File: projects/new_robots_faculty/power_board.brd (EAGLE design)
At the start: 117 x 120.6 mm, 46 parts

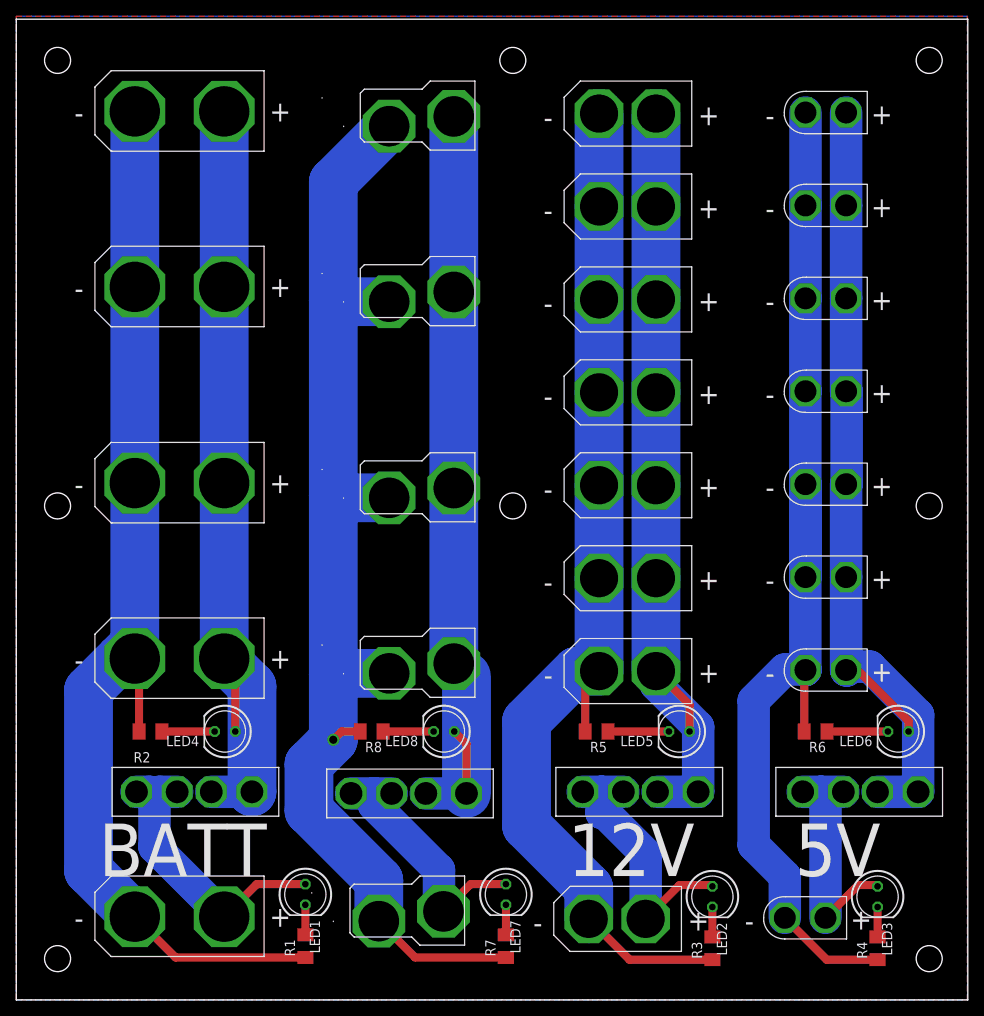
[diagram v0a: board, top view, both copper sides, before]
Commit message: updated power_board
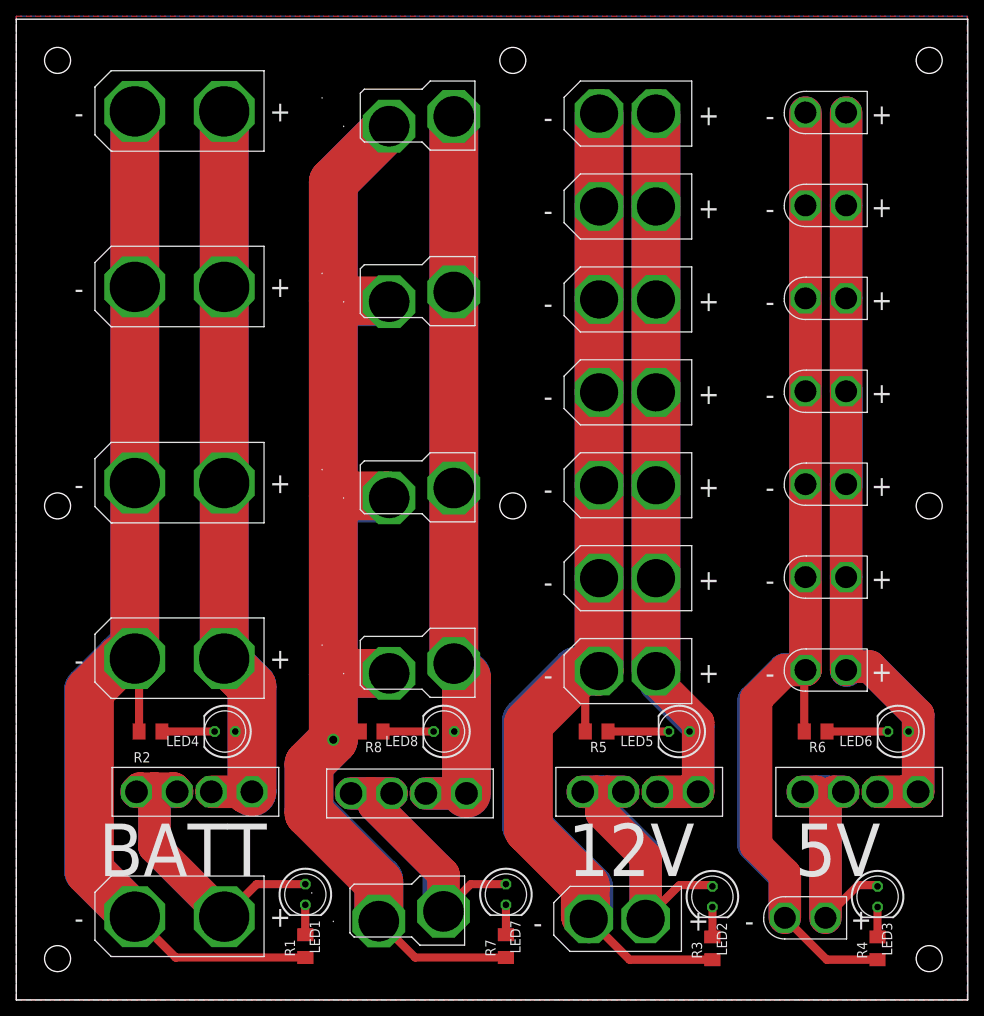
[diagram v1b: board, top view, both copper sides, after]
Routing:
- net N$11: track 147.5 -> 273.8 mm
- net 12V_MINUS: track 133.0 -> 240.0 mm
- net BATT_MINUS: track 137.8 -> 242.4 mm
- net 5V_MINUS: track 137.5 -> 242.0 mm
- net 5V_PLUS: track 106.2 -> 196.0 mm
- net N$12: track 97.2 -> 186.9 mm
- net BATT_PLUS: track 99.7 -> 185.3 mm
- net 12V_PLUS: track 99.7 -> 185.1 mm
- net BATT_RAW: track 35.4 -> 60.1 mm
- net N$9: track 32.4 -> 55.7 mm
- net 12V_RAW: track 33.1 -> 55.9 mm
- net 5V_RAW: track 28.9 -> 48.5 mm
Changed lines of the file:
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@@
 <?xml version="1.0" encoding="utf-8"?>
 <!DOCTYPE eagle SYSTEM "eagle.dtd">
-<eagle version="9.3.2">
+<eagle version="9.6.2">
 <drawing>
 <settings>
@@
 <wire x1="15.11" y1="33.02" x2="15.11" y2="41.46" width="1" layer="1"/>
 <wire x1="15.11" y1="41.46" x2="14.58" y2="41.99" width="1" layer="1"/>
+<wire x1="14.58" y1="10.24" x2="9" y2="15.82" width="6" layer="1"/>
+<wire x1="9" y1="38" x2="13" y2="42" width="6" layer="1"/>
+<wire x1="13" y1="42" x2="14.57" y2="42" width="6" layer="1"/>
+<wire x1="14.57" y1="42" x2="14.58" y2="41.99" width="6" layer="1"/>
+<wire x1="9" y1="15.82" x2="9" y2="38" width="6" layer="1"/>
+<wire x1="14.58" y1="63.58" x2="14.58" y2="41.99" width="6" layer="1"/>
+<wire x1="14.58" y1="63.58" x2="14.58" y2="109.3" width="6" layer="1"/>
 </signal>
 <signal name="BATT_RAW">
@@
 <wire x1="19.79" y1="25.6" x2="17.6" y2="25.6" width="4" layer="16"/>
 <wire x1="17.6" y1="25.6" x2="17" y2="25" width="4" layer="16"/>
+<wire x1="25.58" y1="10.24" x2="17" y2="18.82" width="4" layer="1"/>
+<wire x1="17" y1="18.82" x2="17" y2="26" width="4" layer="1"/>
+<wire x1="17" y1="26" x2="15.19" y2="26" width="4" layer="1"/>
+<wire x1="15.19" y1="26" x2="14.79" y2="25.6" width="4" layer="1"/>
+<wire x1="19.79" y1="25.6" x2="19.39" y2="26" width="4" layer="1"/>
+<wire x1="19.39" y1="26" x2="17" y2="26" width="4" layer="1"/>
 </signal>
 <signal name="BATT_PLUS">
@@
 <contactref element="U$21" pad="C"/>
 <wire x1="25.58" y1="41.99" x2="25.58" y2="63.58" width="6" layer="16"/>
-<wire x1="25.552" y1="41.962" x2="25.58" y2="41.99" width="1" layer="1"/>
 <contactref element="LED4" pad="A"/>
 <wire x1="26.94" y1="33.02" x2="26.94" y2="40.574" width="1" layer="1"/>
 <wire x1="26.94" y1="40.574" x2="25.552" y2="41.962" width="1" layer="1"/>
-<wire x1="23.99" y1="25.6" x2="28.99" y2="25.6" width="4" layer="16"/>
 <wire x1="28.99" y1="25.6" x2="29" y2="25.61" width="6" layer="16"/>
 <wire x1="29" y1="38.57" x2="25.58" y2="41.99" width="6" layer="16"/>
@@
 <wire x1="25.58" y1="109.3" x2="25.58" y2="87.71" width="6" layer="16"/>
 <wire x1="25.58" y1="87.71" x2="25.58" y2="63.58" width="6" layer="16"/>
+<wire x1="25.58" y1="109.3" x2="25.58" y2="41.99" width="6" layer="1"/>
+<wire x1="25.58" y1="41.99" x2="25.552" y2="41.962" width="6" layer="1"/>
+<wire x1="28.99" y1="25.6" x2="28.99" y2="38.524" width="6" layer="1"/>
+<wire x1="28.99" y1="38.524" x2="25.552" y2="41.962" width="6" layer="1"/>
+<wire x1="23.99" y1="25.6" x2="27.4" y2="25.6" width="4" layer="1"/>
+<wire x1="27.4" y1="25.6" x2="28" y2="25" width="4" layer="1"/>
+<wire x1="28" y1="25" x2="28.39" y2="25" width="4" layer="1"/>
+<wire x1="28.39" y1="25" x2="28.99" y2="25.6" width="4" layer="1"/>
 </signal>
 <signal name="N$5">
@@
 <wire x1="72.39" y1="23" x2="72" y2="23" width="4" layer="16"/>
 <wire x1="72" y1="23" x2="72" y2="25.6" width="4" layer="16"/>
+<wire x1="77.42" y1="9.97" x2="77.42" y2="17.58" width="4" layer="1"/>
+<wire x1="77.42" y1="17.58" x2="72" y2="23" width="4" layer="1"/>
+<wire x1="72" y1="23" x2="72" y2="25" width="4" layer="1"/>
+<wire x1="72" y1="25" x2="71.4" y2="25.6" width="4" layer="1"/>
+<wire x1="71.4" y1="25.6" x2="69.68" y2="25.6" width="4" layer="1"/>
+<wire x1="74.68" y1="25.6" x2="72.6" y2="25.6" width="4" layer="1"/>
+<wire x1="72.6" y1="25.6" x2="72" y2="25" width="4" layer="1"/>
 </signal>
 <signal name="N$8">
@@
 <wire x1="99.54" y1="10.1" x2="99.54" y2="25.06" width="4" layer="16"/>
 <wire x1="99.54" y1="25.06" x2="99" y2="25.6" width="4" layer="16"/>
+<wire x1="99.54" y1="10.1" x2="99.54" y2="24.46" width="4" layer="1"/>
+<wire x1="98.4" y1="25.6" x2="96.74" y2="25.6" width="4" layer="1"/>
+<wire x1="99.54" y1="24.46" x2="98.4" y2="25.6" width="4" layer="1"/>
+<wire x1="101.74" y1="25.6" x2="100.6" y2="25.6" width="4" layer="1"/>
+<wire x1="100.6" y1="25.6" x2="100" y2="25" width="4" layer="1"/>
 </signal>
 <signal name="5V_PLUS">
@@
 <wire x1="109.76" y1="34.29" x2="109.76" y2="33.02" width="1" layer="1"/>
 <wire x1="103.41" y1="40.64" x2="109.76" y2="34.29" width="1" layer="1"/>
-<wire x1="105.94" y1="25.6" x2="110.94" y2="25.6" width="4" layer="16"/>
 <wire x1="110.94" y1="25.6" x2="110.94" y2="35.06" width="4" layer="16"/>
 <wire x1="110.94" y1="35.06" x2="105" y2="41" width="4" layer="16"/>
 <wire x1="105" y1="41" x2="102.62" y2="41" width="4" layer="16"/>
 <wire x1="102.62" y1="41" x2="102.14" y2="40.52" width="4" layer="16"/>
+<wire x1="105.94" y1="25.6" x2="109.6" y2="25.6" width="4" layer="1"/>
+<wire x1="109.6" y1="25.6" x2="110" y2="26" width="4" layer="1"/>
+<wire x1="110" y1="26" x2="110.54" y2="26" width="4" layer="1"/>
+<wire x1="110.54" y1="26" x2="110.94" y2="25.6" width="4" layer="1"/>
+<wire x1="102.08" y1="40.58" x2="102.08" y2="109.16" width="4" layer="1"/>
+<wire x1="110.94" y1="25.6" x2="110.94" y2="35.06" width="4" layer="1"/>
+<wire x1="110.94" y1="35.06" x2="105" y2="41" width="4" layer="1"/>
+<wire x1="105" y1="41" x2="102.5" y2="41" width="4" layer="1"/>
+<wire x1="102.5" y1="41" x2="102.14" y2="40.64" width="4" layer="1"/>
 </signal>
 <signal name="5V_MINUS">
@@
 <wire x1="97.08" y1="53.28" x2="97.06" y2="53.26" width="4" layer="16"/>
 <wire x1="97.08" y1="52.01" x2="97.08" y2="63.44" width="4" layer="16"/>
+<wire x1="97.08" y1="109.16" x2="97.08" y2="40.58" width="4" layer="1"/>
+<wire x1="97.08" y1="40.58" x2="94.58" y2="40.58" width="4" layer="1"/>
+<wire x1="94.58" y1="40.58" x2="91" y2="37" width="4" layer="1"/>
+<wire x1="91" y1="19" x2="91" y2="37" width="4" layer="1"/>
+<wire x1="94.54" y1="10.1" x2="94.54" y2="15.46" width="4" layer="1"/>
+<wire x1="94.54" y1="15.46" x2="91" y2="19" width="4" layer="1"/>
 </signal>
 <signal name="N$3">
@@
 <wire x1="82.82" y1="33.02" x2="82.82" y2="36.32" width="1" layer="1"/>
 <wire x1="82.82" y1="36.32" x2="78.69" y2="40.45" width="1" layer="1"/>
-<wire x1="78.88" y1="25.6" x2="83.88" y2="25.6" width="4" layer="16"/>
 <wire x1="83.88" y1="25.6" x2="83.88" y2="33.59" width="4" layer="16"/>
 <wire x1="83.88" y1="33.59" x2="78.69" y2="38.78" width="4" layer="16"/>
+<wire x1="78.69" y1="40.45" x2="78.69" y2="109.03" width="6" layer="1"/>
+<wire x1="78.88" y1="25.6" x2="82.6" y2="25.6" width="4" layer="1"/>
+<wire x1="82.6" y1="25.6" x2="83" y2="26" width="4" layer="1"/>
+<wire x1="83" y1="26" x2="83.48" y2="26" width="4" layer="1"/>
+<wire x1="83.48" y1="26" x2="83.88" y2="25.6" width="4" layer="1"/>
+<wire x1="83.88" y1="25.6" x2="83.88" y2="34.12" width="4" layer="1"/>
+<wire x1="79" y1="39" x2="79" y2="40" width="4" layer="1"/>
+<wire x1="83.88" y1="34.12" x2="79" y2="39" width="4" layer="1"/>
 </signal>
 <signal name="12V_MINUS">
@@
 <wire x1="71.69" y1="74.74" x2="71.69" y2="86.17" width="6" layer="16"/>
 <wire x1="71.69" y1="86.17" x2="71.69" y2="97.6" width="6" layer="16"/>
+<wire x1="71.69" y1="109.03" x2="71.69" y2="40.45" width="6" layer="1"/>
+<wire x1="71.69" y1="40.45" x2="69.45" y2="40.45" width="6" layer="1"/>
+<wire x1="69.45" y1="40.45" x2="63" y2="34" width="6" layer="1"/>
+<wire x1="63" y1="34" x2="63" y2="21" width="6" layer="1"/>
+<wire x1="63" y1="21" x2="70" y2="14" width="6" layer="1"/>
+<wire x1="70" y1="14" x2="70" y2="12" width="6" layer="1"/>
+<wire x1="70.42" y1="9.97" x2="70" y2="10.39" width="6" layer="1"/>
+<wire x1="70" y1="10.39" x2="70" y2="12" width="6" layer="1"/>
 </signal>
 <signal name="N$2">
@@
 <wire x1="52" y1="16" x2="44" y2="24" width="4" layer="16"/>
 <wire x1="44" y1="24" x2="44" y2="25.4" width="4" layer="16"/>
+<wire x1="52.55" y1="10.89" x2="52.55" y2="15.45" width="4" layer="1"/>
+<wire x1="44" y1="24" x2="44" y2="25" width="4" layer="1"/>
+<wire x1="44" y1="25" x2="43.6" y2="25.4" width="4" layer="1"/>
+<wire x1="43.6" y1="25.4" x2="41.18" y2="25.4" width="4" layer="1"/>
+<wire x1="52.55" y1="15.45" x2="44" y2="24" width="4" layer="1"/>
+<wire x1="46.18" y1="25.4" x2="43.6" y2="25.4" width="4" layer="1"/>
 </signal>
 <signal name="N$10">
@@
 <wire x1="45.87" y1="40.17" x2="39.17" y2="40.17" width="6" layer="16"/>
 <wire x1="39.17" y1="40.17" x2="39" y2="40" width="4" layer="16"/>
+<wire x1="44.6" y1="9.69" x2="44.6" y2="14.4" width="6" layer="1"/>
+<wire x1="44.6" y1="14.4" x2="36" y2="23" width="6" layer="1"/>
+<wire x1="36" y1="23" x2="36" y2="29" width="6" layer="1"/>
+<wire x1="39" y1="100.61" x2="45.87" y2="107.48" width="6" layer="1"/>
+<wire x1="36" y1="29" x2="39" y2="32" width="6" layer="1"/>
+<wire x1="39" y1="32" x2="39" y2="40" width="6" layer="1"/>
+<wire x1="39" y1="40" x2="39" y2="62" width="6" layer="1"/>
+<wire x1="39" y1="62" x2="39" y2="86" width="6" layer="1"/>
+<wire x1="39" y1="86" x2="39" y2="100.61" width="6" layer="1"/>
+<wire x1="45.87" y1="85.89" x2="45.76" y2="86" width="6" layer="1"/>
+<wire x1="45.76" y1="86" x2="39" y2="86" width="6" layer="1"/>
+<wire x1="45.87" y1="61.76" x2="45.63" y2="62" width="6" layer="1"/>
+<wire x1="45.63" y1="62" x2="39" y2="62" width="6" layer="1"/>
+<wire x1="45.87" y1="40.17" x2="39.17" y2="40.17" width="6" layer="1"/>
+<wire x1="39.17" y1="40.17" x2="39" y2="40" width="6" layer="1"/>
 </signal>
 <signal name="N$12">
@@
 <wire x1="53.82" y1="62.96" x2="53.82" y2="87.09" width="6" layer="16"/>
 <wire x1="53.82" y1="87.09" x2="53.82" y2="108.68" width="6" layer="16"/>
+<wire x1="55.38" y1="25.4" x2="55.38" y2="39.62" width="6" layer="1"/>
+<wire x1="53.82" y1="41.18" x2="53.82" y2="62.96" width="6" layer="1"/>
+<wire x1="55.38" y1="39.62" x2="53.82" y2="41.18" width="6" layer="1"/>
+<wire x1="53.82" y1="62.96" x2="53.82" y2="108.68" width="6" layer="1"/>
+<wire x1="50.38" y1="25.4" x2="55.6" y2="25.4" width="4" layer="1"/>
+<wire x1="55.6" y1="25.4" x2="56" y2="25" width="4" layer="1"/>
 </signal>
 <signal name="N$13">

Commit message: miniaturized chassis board
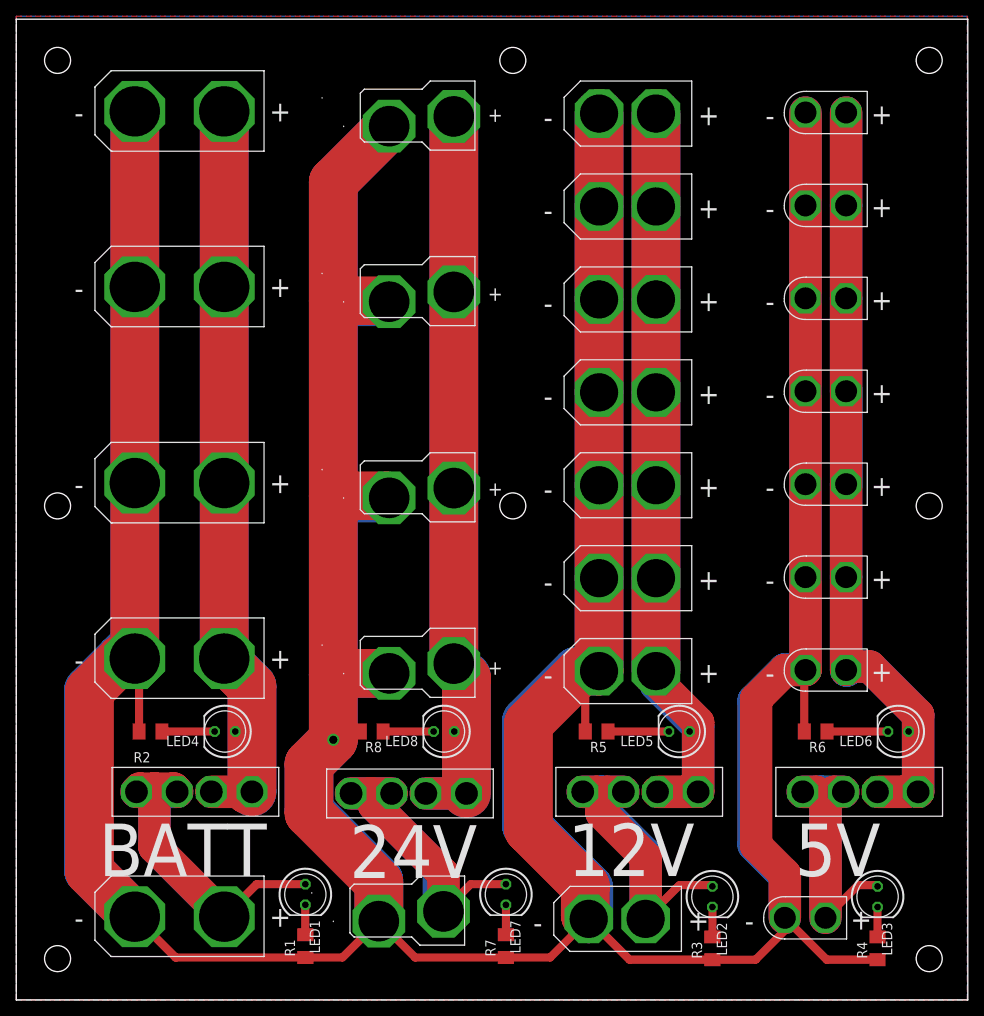
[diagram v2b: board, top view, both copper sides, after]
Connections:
- removed net 5V_MINUS: R4.1, R6.2, U$13.MINUS, U$14.MINUS, U$15.MINUS, U$16.MINUS, U$17.MINUS, U$18.MINUS, U$19.MINUS, U$20.MINUS
- removed net BATT_MINUS: R1.1, R2.2, U$1.MINUS, U$2.MINUS, U$24.MINUS, U$3.MINUS, U$4.MINUS
- removed net N$11: R7.1, R8.2, U$25.P-2, U$26.P-2, U$27.P-2, U$28.P-2, U$29.P-2
- net 12V_MINUS: now also R1.1, R2.2, R4.1, R6.2, R7.1, R8.2, U$1.MINUS, U$13.MINUS, U$14.MINUS, U$15.MINUS, U$16.MINUS, U$17.MINUS, U$18.MINUS, U$19.MINUS, U$2.MINUS, U$20.MINUS, U$24.MINUS, U$25.P-2, U$26.P-2, U$27.P-2, U$28.P-2, U$29.P-2, U$3.MINUS, U$4.MINUS
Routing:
- net 12V_MINUS: track 240.0 -> 1033.3 mm, vias 0 -> 1
- net N$11: track 273.8 -> 0.00 mm, vias 1 -> 0
- net BATT_MINUS: track 242.4 -> 0.00 mm
- net 5V_MINUS: track 242.0 -> 0.00 mm
- net N$12: track 186.9 -> 186.3 mm
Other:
- board text added: "+"

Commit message: updated asgard power board
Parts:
- added U$31, U$32, U$33: T-PLUG_CONNECTOR, con-T-plug:T_PLUG_CONNECTOR
- added U$34: XT90, XT_connectors:XT90_FOOTPRINT
- moved U$24 5.00 mm to (30.5, 63.6)
- moved U$4 4.50 mm to (30.5, 97.2)
- moved U$28 0.50 mm to (56.4, 67.8)
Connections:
- net 12V_MINUS: now also U$31.P-2, U$32.P-2, U$33.P-2, U$34.MINUS
- net BATT_PLUS: now also U$34.PLUS
- net N$12: now also U$31.P-1, U$32.P-1, U$33.P-1
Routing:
- net 12V_MINUS: track 1033.3 -> 1082.3 mm
- net BATT_PLUS: track 185.3 -> 206.8 mm
- net N$12: track 186.3 -> 192.8 mm
- net N$15: track 0.00 -> 5.00 mm
- net N$14: track 0.00 -> 5.00 mm
- net N$11: track 0.00 -> 5.00 mm
- net 12V_PLUS: track 185.1 -> 183.9 mm
- net 5V_RAW: track 48.5 -> 47.6 mm
